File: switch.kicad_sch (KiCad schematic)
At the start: 3 parts

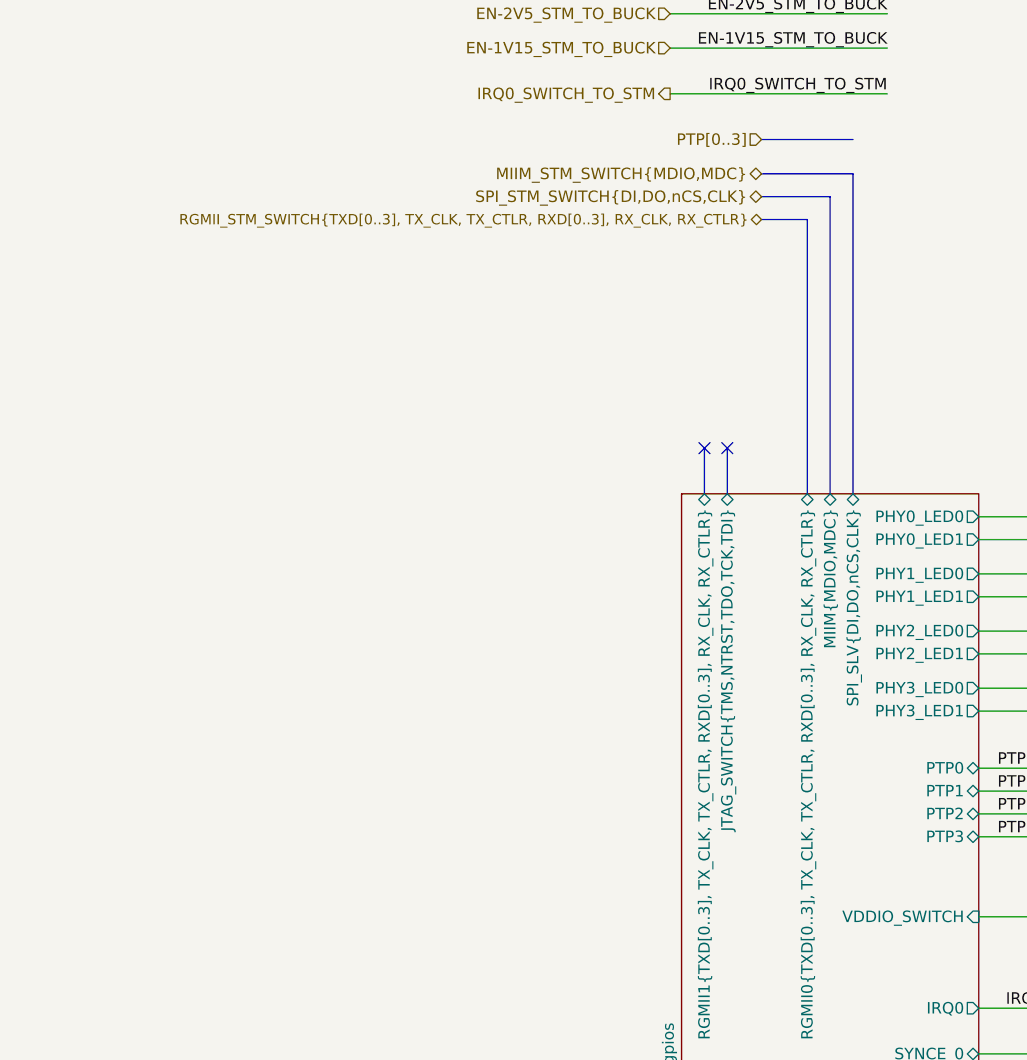
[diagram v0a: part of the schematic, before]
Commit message: connects SPI from STM to Switch. Refs: #1
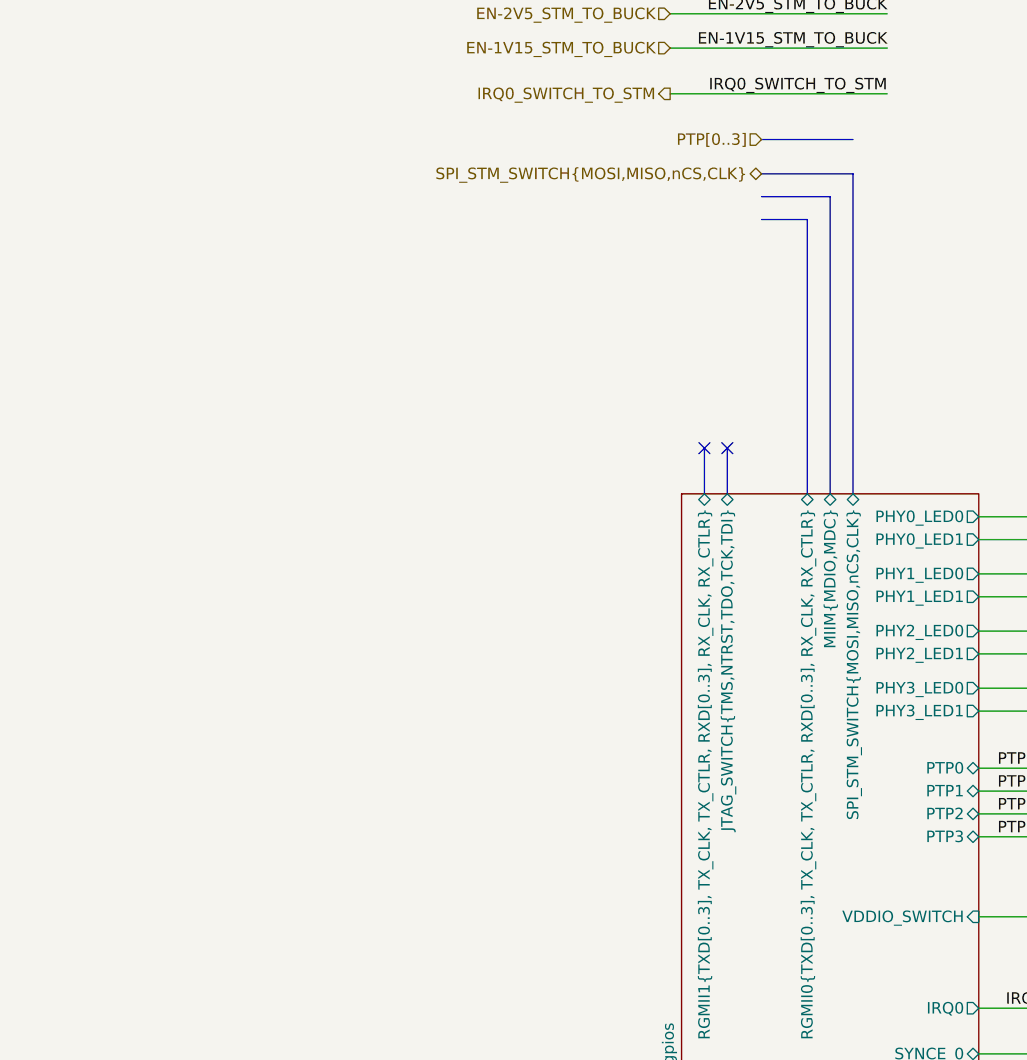
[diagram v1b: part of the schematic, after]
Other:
- sheet switch_gpios ports: added SPI_STM_SWITCH{MOSI,MISO,nCS,CLK}; removed SPI_SLV{DI,DO,nCS,CLK}
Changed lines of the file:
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@@
 		)
 	)
-	(hierarchical_label "SPI_STM_SWITCH{DI,DO,nCS,CLK}"
-		(shape bidirectional)
-		(at 82.55 59.69 180)
-		(effects
-			(font
-				(size 1.27 1.27)
-			)
-			(justify right)
-		)
-	)
-	(hierarchical_label "MIIM_STM_SWITCH{MDIO,MDC}"
+	(hierarchical_label "SPI_STM_SWITCH{MOSI,MISO,nCS,CLK}"
 		(shape bidirectional)
 		(at 82.55 57.15 180)
@@
 			(font
 				(size 1.27 1.27)
-			)
-			(justify right)
-		)
-	)
-	(hierarchical_label "RGMII_STM_SWITCH{TXD[0..3], TX_CLK, TX_CTLR, RXD[0..3], RX_CLK, RX_CTLR}"
-		(shape bidirectional)
-		(at 82.55 62.23 180)
-		(effects
-			(font
-				(size 1.143 1.143)
 			)
 			(justify right)
@@
 			)
 		)
-		(pin "SPI_SLV{DI,DO,nCS,CLK}" bidirectional
+		(pin "SPI_STM_SWITCH{MOSI,MISO,nCS,CLK}" bidirectional
 			(at 92.71 92.71 90)
 			(effects

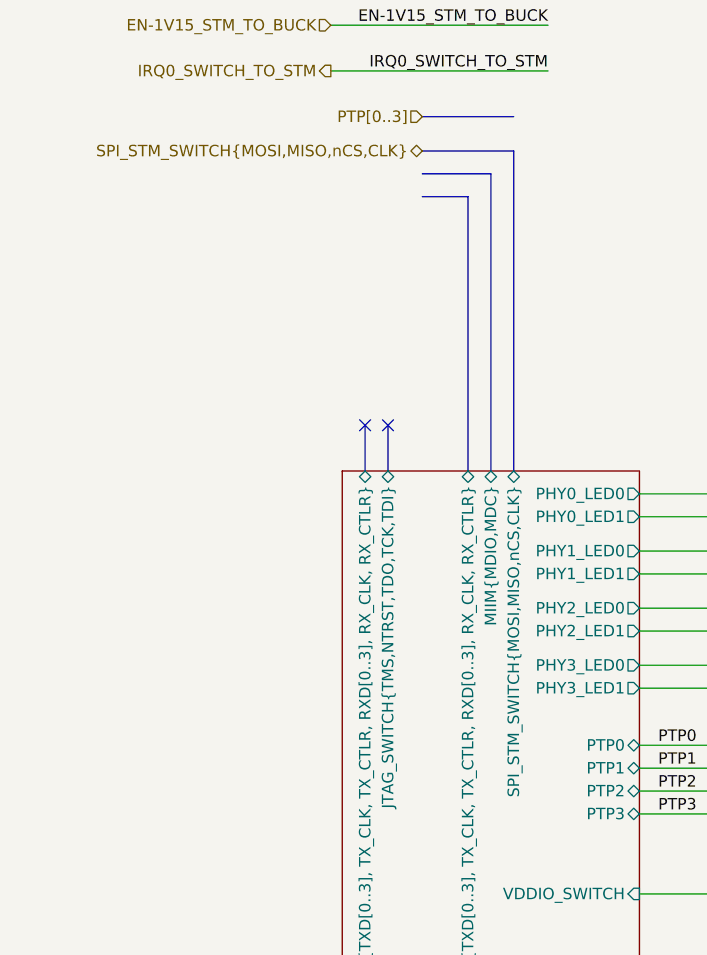
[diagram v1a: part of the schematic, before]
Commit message: connects MIIM bus from STM to Switch. Refs: #1
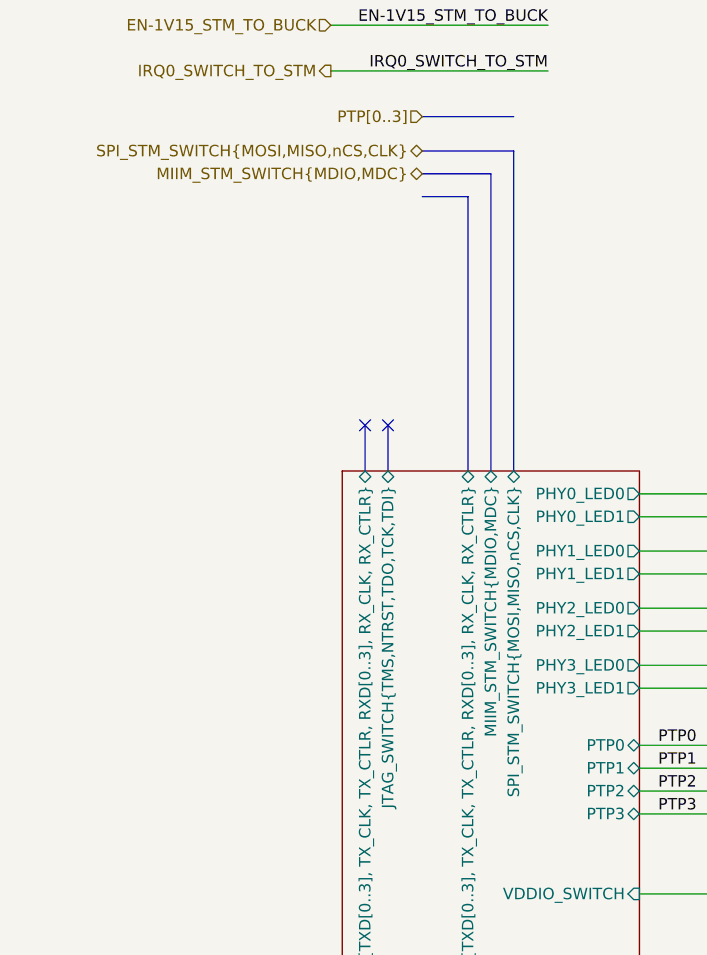
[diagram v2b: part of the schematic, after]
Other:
- sheet switch_gpios ports: added MIIM_STM_SWITCH{MDIO,MDC}; removed MIIM{MDIO,MDC}
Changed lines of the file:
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@@
+		)
+	)
+	(hierarchical_label "MIIM_STM_SWITCH{MDIO,MDC}"
+		(shape bidirectional)
+		(at 82.55 59.69 180)
+		(effects
+			(font
+				(size 1.27 1.27)
+			)
+			(justify right)
 		)
 	)
@@
 			)
 		)
-		(pin "MIIM{MDIO,MDC}" bidirectional
+		(pin "MIIM_STM_SWITCH{MDIO,MDC}" bidirectional
 			(at 90.17 92.71 90)
 			(effects

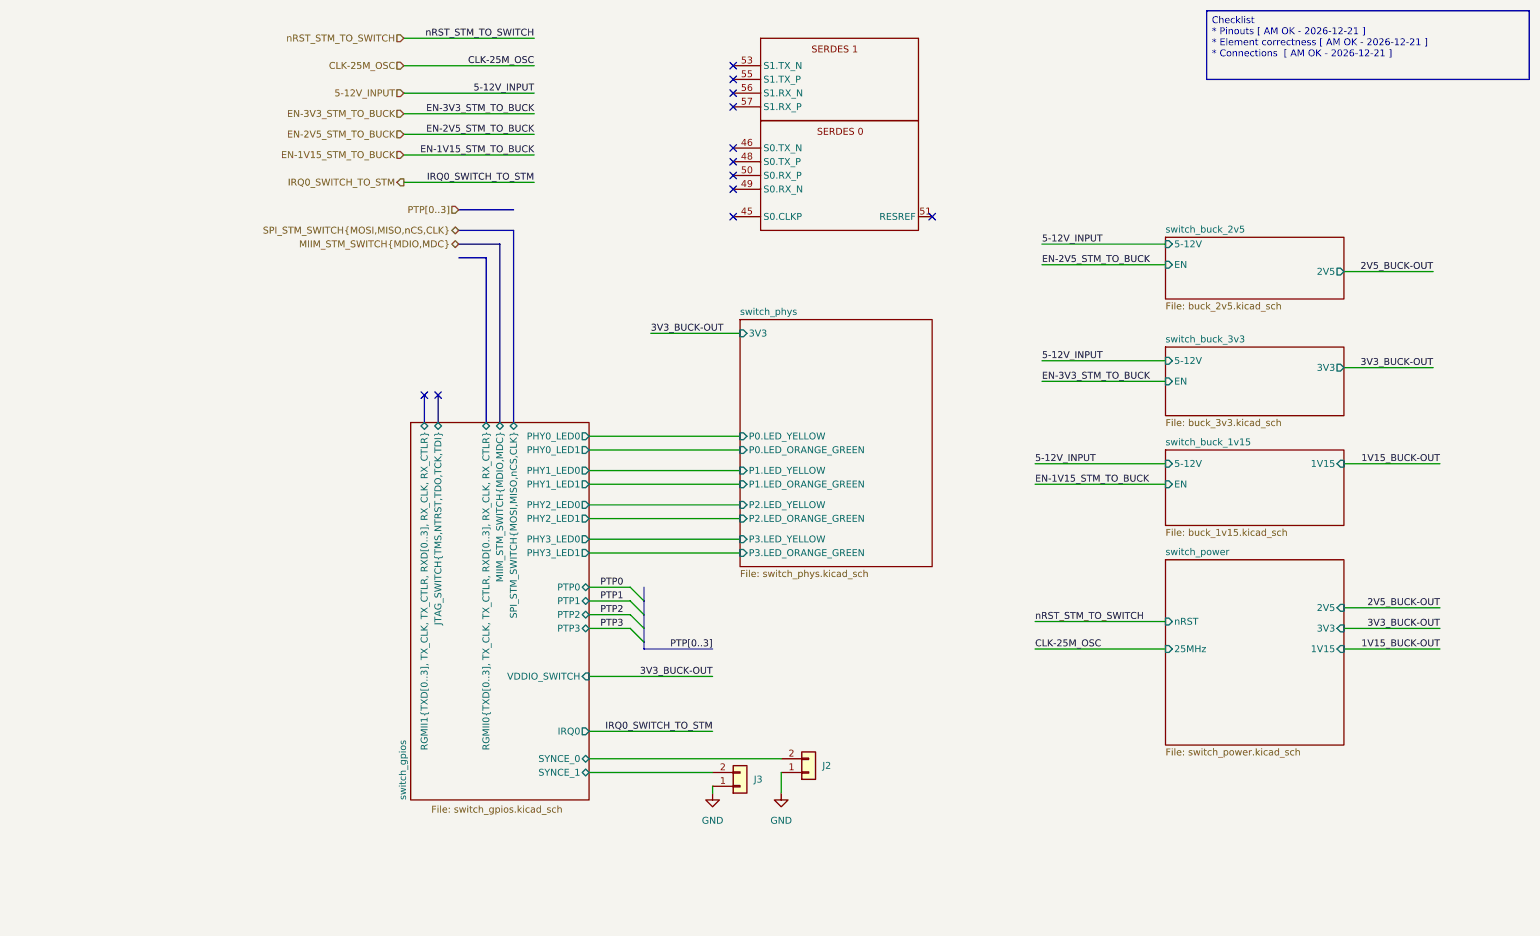
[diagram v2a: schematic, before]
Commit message: connects RGMII1 bus between Switch and STM. Refs: #1
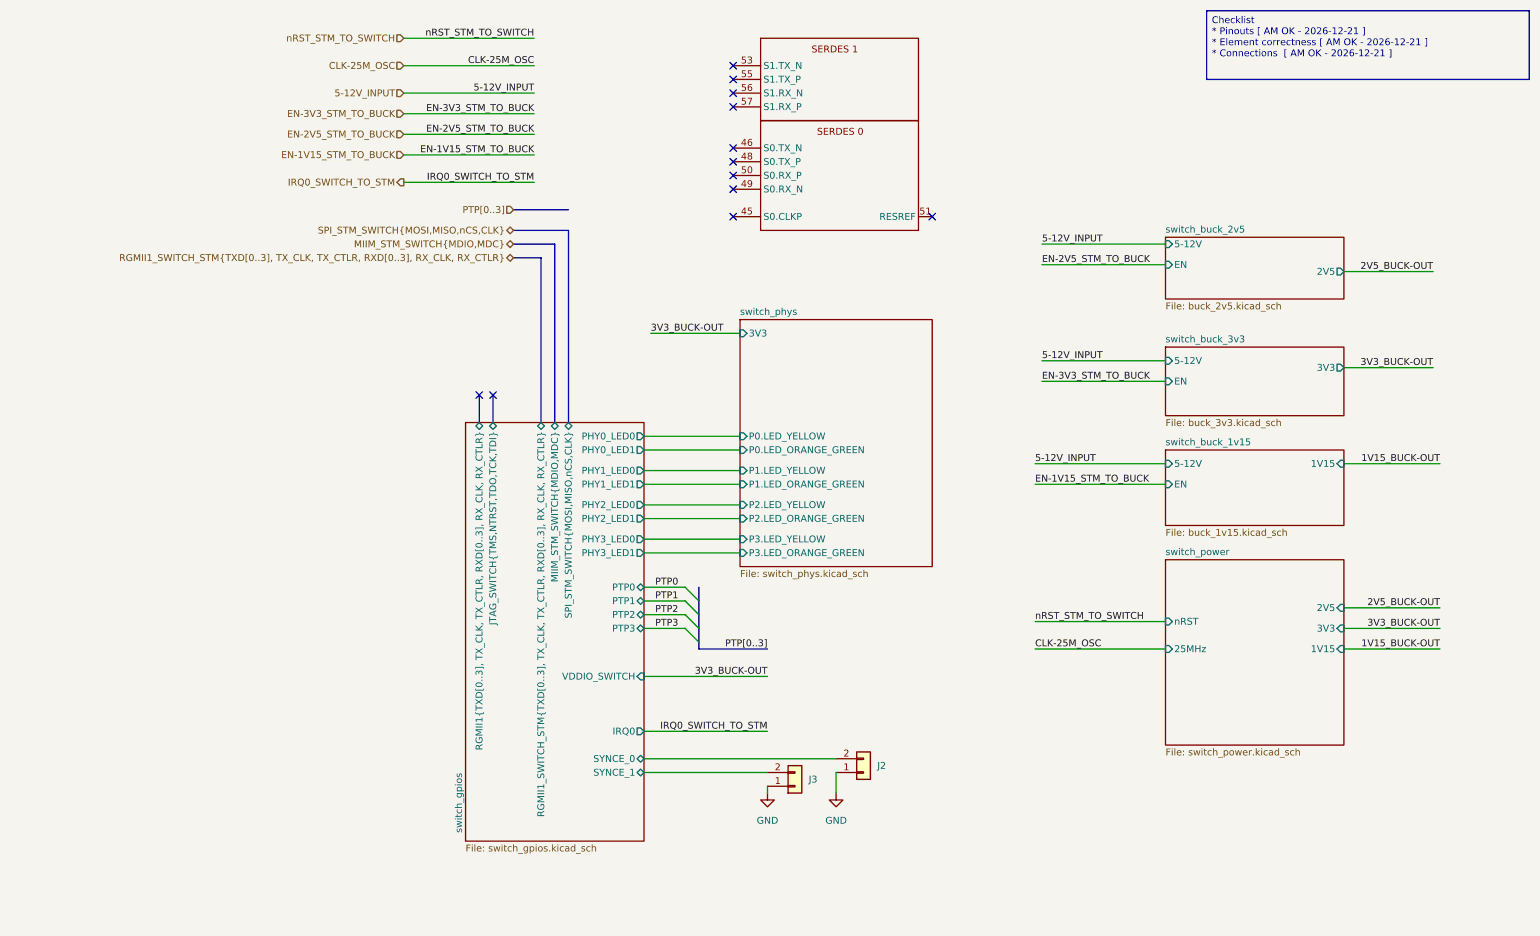
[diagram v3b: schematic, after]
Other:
- sheet switch_gpios ports: added RGMII1_SWITCH_STM{TXD[0..3], TX_CLK, TX_CTLR, RXD[0..3], RX_CLK, RX_CTLR}; removed RGMII0{TXD[0..3], TX_CLK, TX_CTLR, RXD[0..3], RX_CLK, RX_CTLR}
- moved on the sheet: J2, J3
